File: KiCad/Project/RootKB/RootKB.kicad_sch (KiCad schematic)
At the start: 72 parts, among them J1 OLED-128x32, SW1 Switch, U1 Arduino_Pro_Micro, U2 TRRS

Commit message: update pcb
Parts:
- removed TP1, TP2: TestPoint, TestPoint:TestPoint_Pad_1.5x1.5mm, symbol Connector:TestPoint

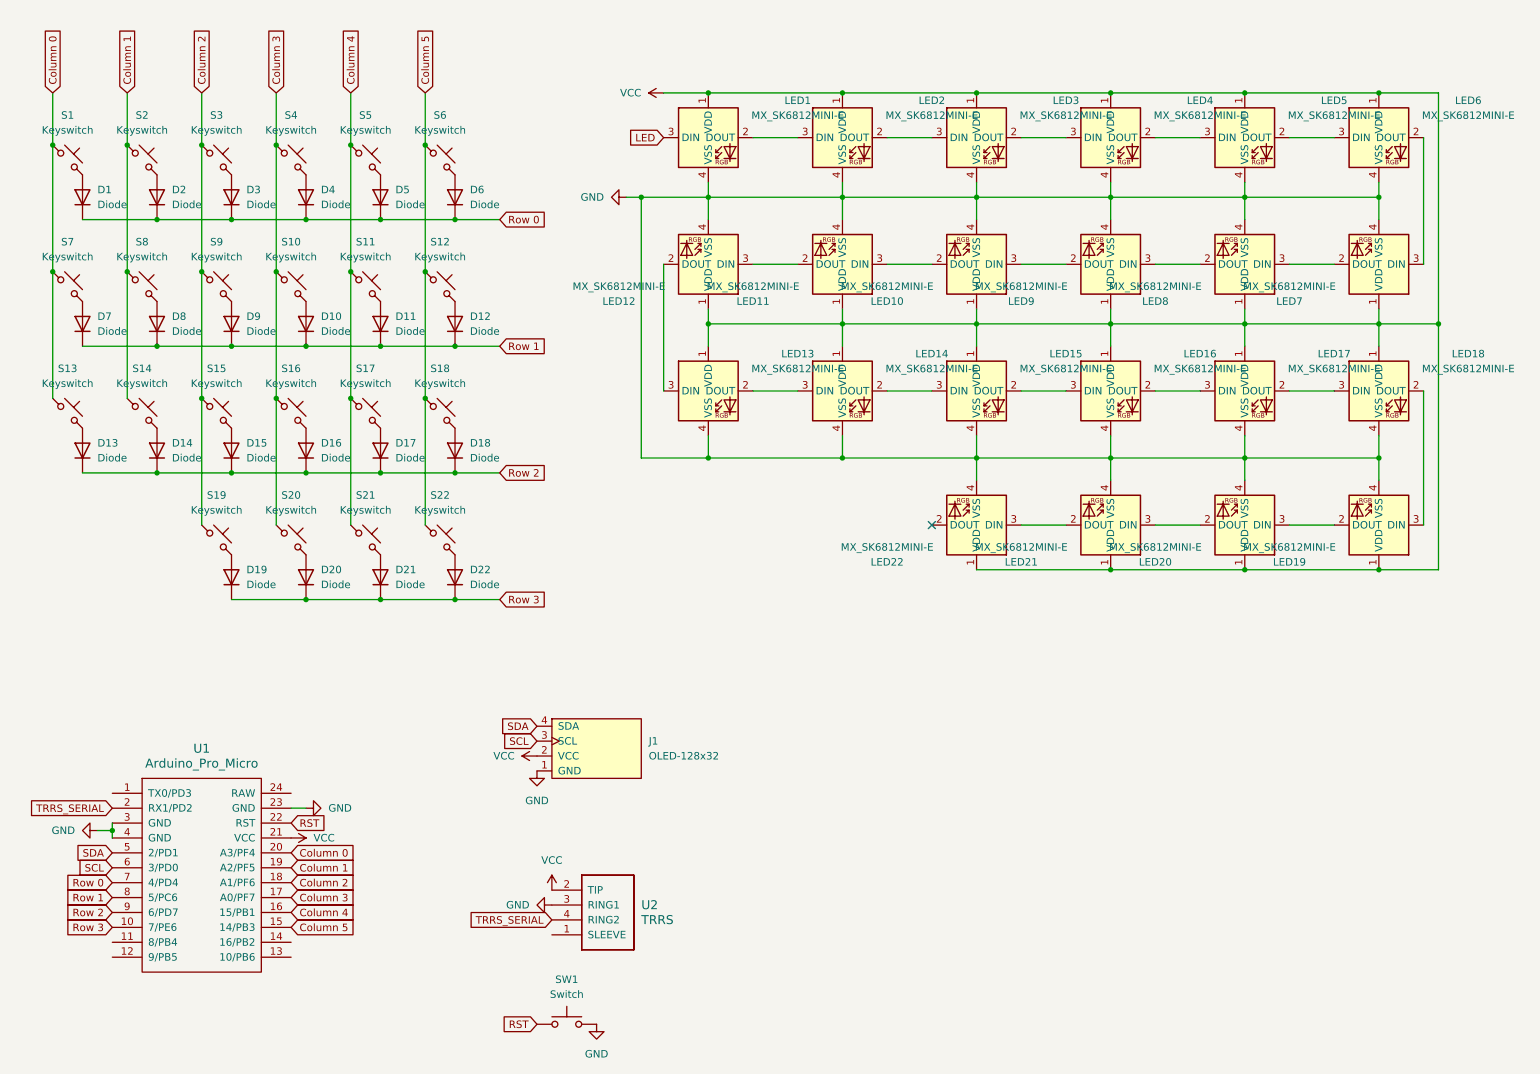
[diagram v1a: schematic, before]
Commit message: add right side
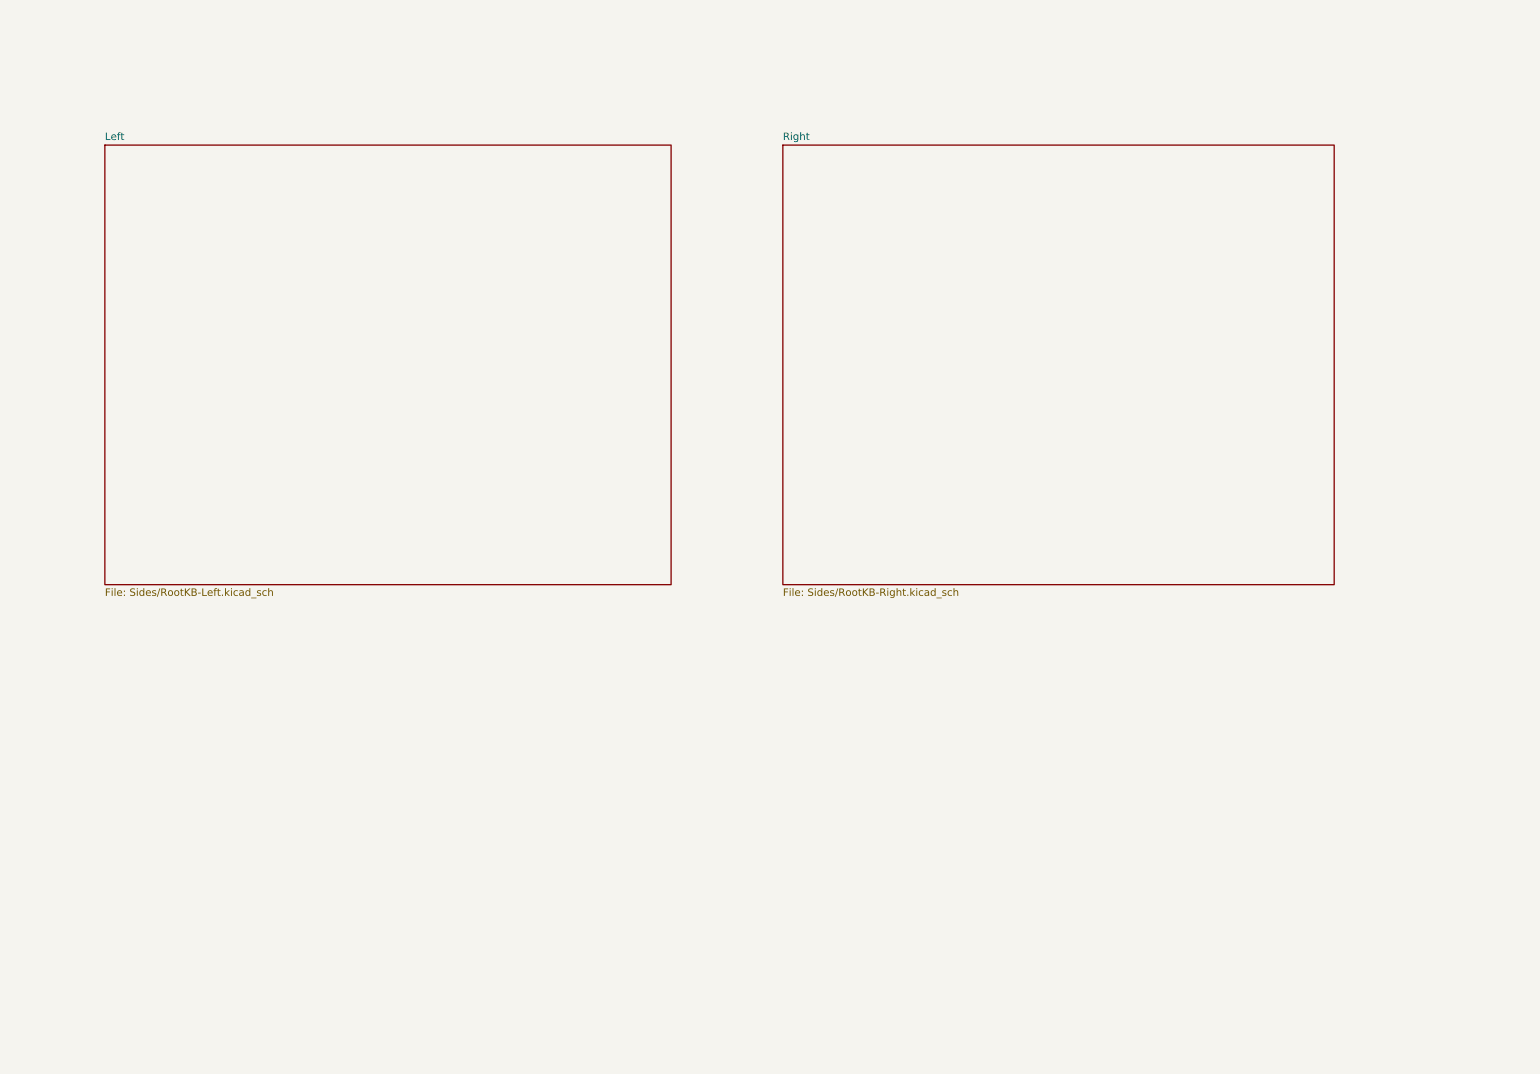
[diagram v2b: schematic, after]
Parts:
- removed D1, D10, D11, D12, D13, D14, D15, D16, D17, D18, D19, D2, D20, D21, D22, D3, D4, D5, D6, D7, D8, D9: Diode, Diode_SMD:D_SOD-123F, symbol ScottoKeebs:Placeholder_Diode
- removed J1: OLED-128x32, display:OLED-128x32-cutout, symbol display:OLED-128x32
- removed LED1, LED10, LED11, LED12, LED13, LED14, LED15, LED16, LED17, LED18, LED19, LED2, LED20, LED21, LED22, LED3, LED4, LED5, LED6, LED7, LED8, LED9: MX_SK6812MINI-E, PCM_marbastlib-mx:LED_MX_6028R, symbol PCM_marbastlib-mx:MX_SK6812MINI-E
- removed S1, S10, S11, S12, S13, S14, S15, S16, S17, S18, S19, S2, S22, S3, S4, S5, S6, S7, S8, S9: Keyswitch, PCM_Switch_Keyboard_Hotswap_Kailh:SW_Hotswap_Kailh_MX_1.00u, symbol ScottoKeebs:Placeholder_Keyswitch
- removed S20, S21: Keyswitch, PCM_Switch_Keyboard_Hotswap_Kailh:SW_Hotswap_Kailh_MX_1.25u_90deg, symbol ScottoKeebs:Placeholder_Keyswitch
- removed SW1: Switch, ScottoKeebs_Components:Button_MJTP1250, symbol ScottoKeebs:Placeholder_Switch
- removed U1: Arduino_Pro_Micro, ScottoKeebs_MCU:Arduino_Pro_Micro, symbol ScottoKeebs:MCU_Arduino_Pro_Micro
- removed U2: TRRS, ScottoKeebs_Components:TRRS_PJ-320A, symbol ScottoKeebs:Placeholder_TRRS
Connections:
- no-connect marks 1 -> 0
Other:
- added sheet Left (Sides/RootKB-Left.kicad_sch)
- added sheet Right (Sides/RootKB-Right.kicad_sch)
